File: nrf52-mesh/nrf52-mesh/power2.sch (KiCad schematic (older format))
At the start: 19 parts, among them J4 Conn_01x02_Male, J5 Conn_01x02_Male, U1 TLV62568DBV, U3 FAN5341, U6 CP2102N-A01-GQFN24, X1 USBFCI_10103594

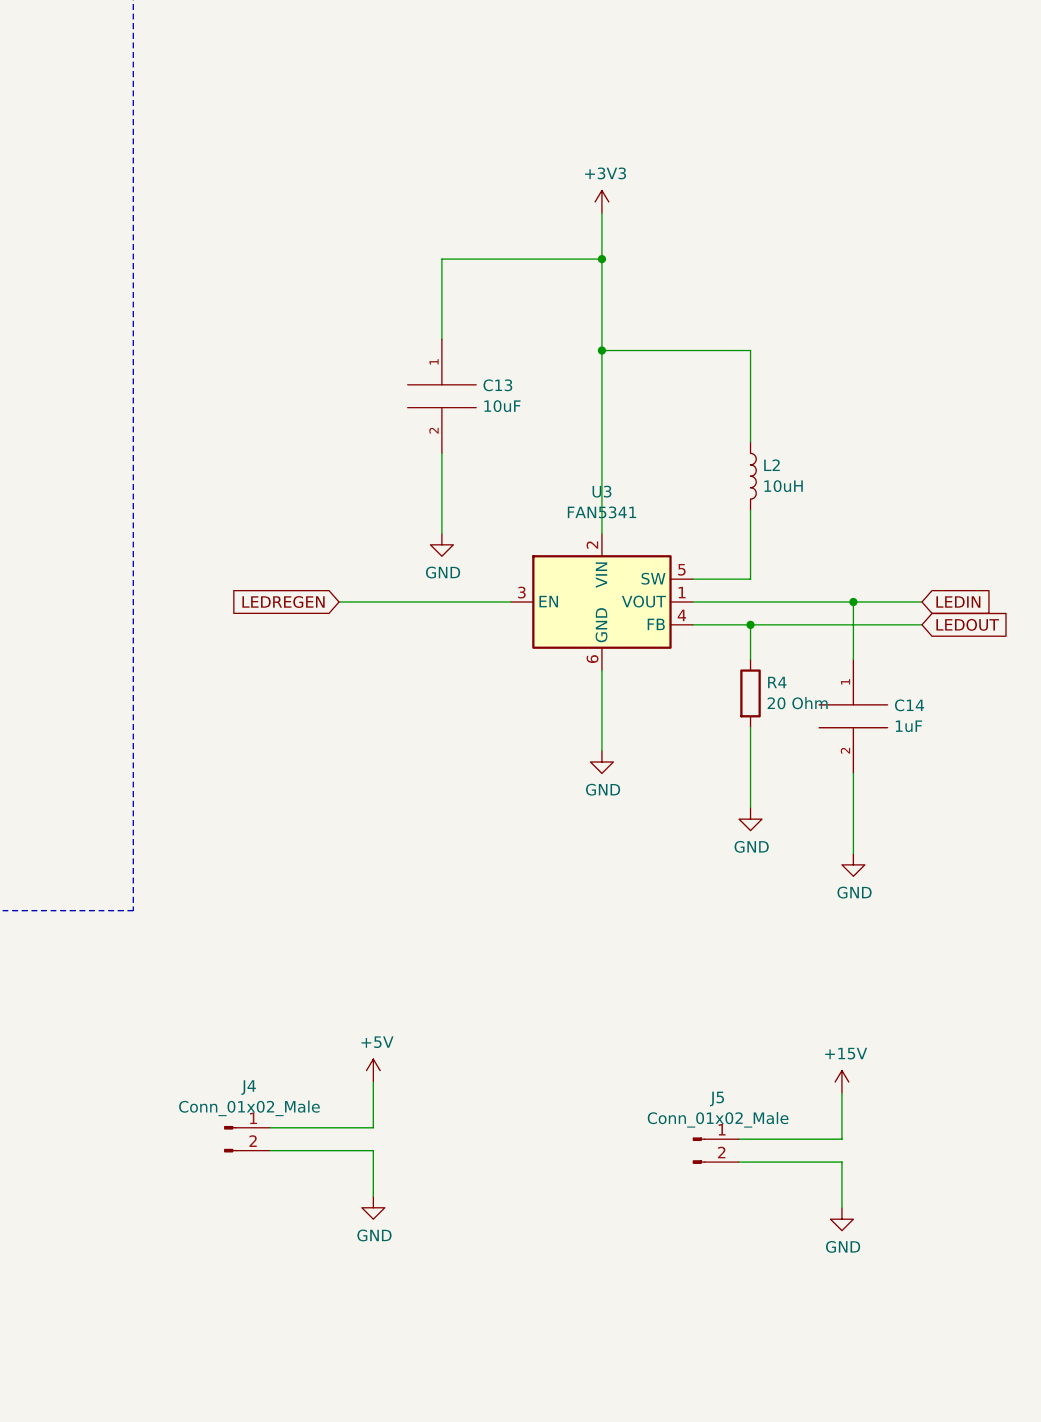
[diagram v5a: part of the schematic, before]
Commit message: nRF52 + ESP WROOM
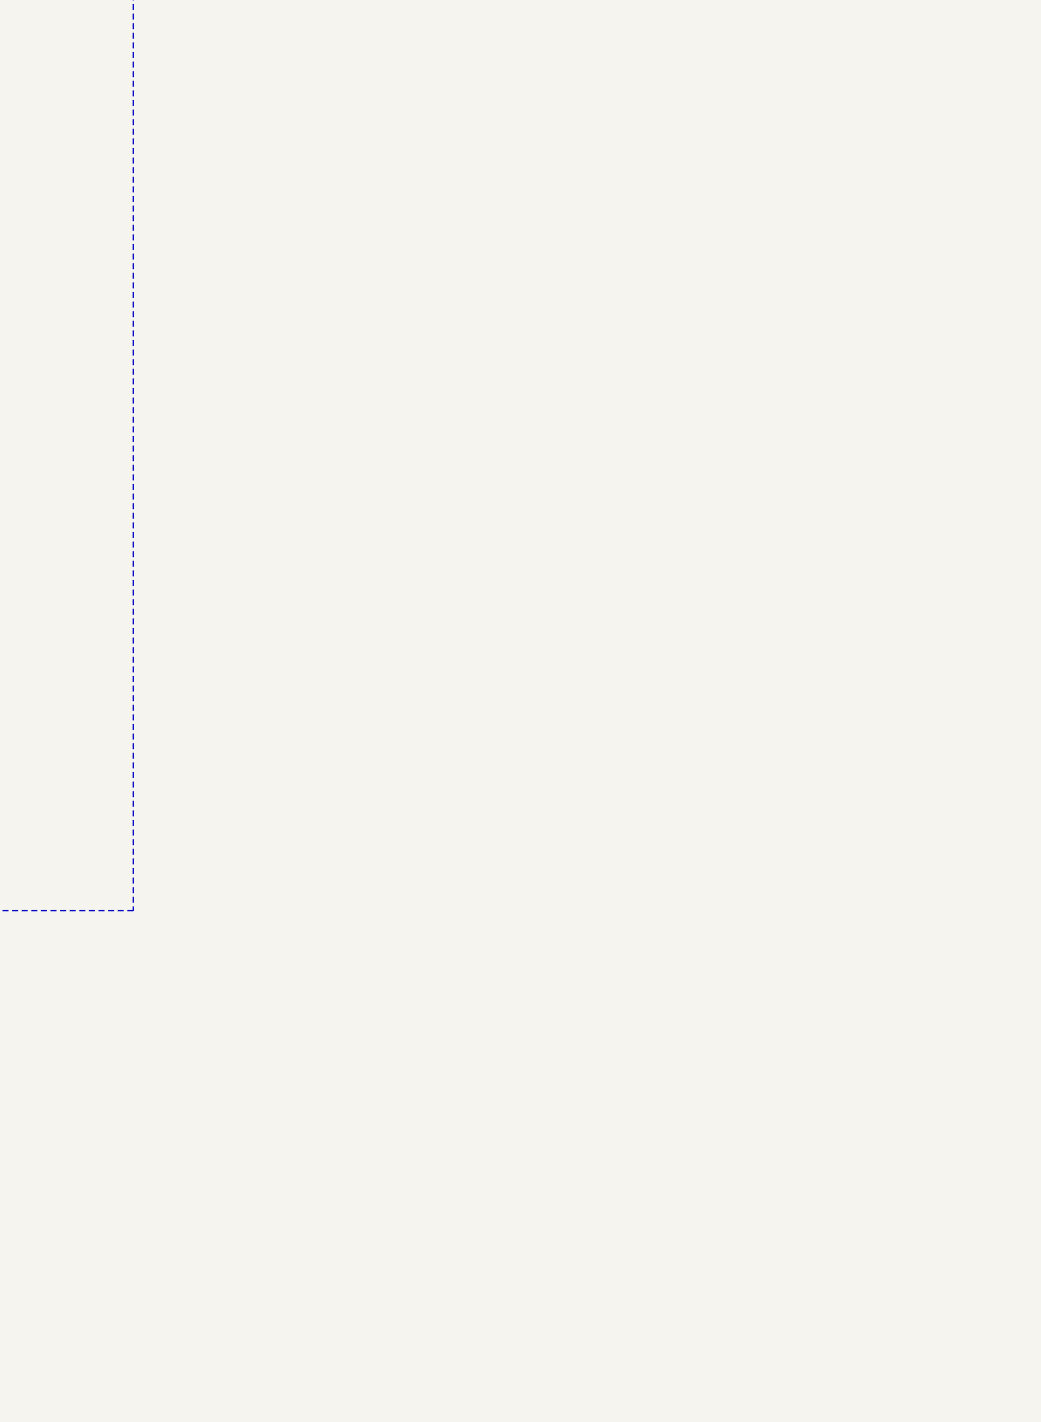
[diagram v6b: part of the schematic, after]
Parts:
- removed C13: 10uF, Capacitor_SMD:C_0603_1608Metric, symbol pspice:C
- removed C14: 1uF, Capacitor_SMD:C_0402_1005Metric, symbol pspice:C
- removed J4, J5: Conn_01x02_Male, Connector_PinHeader_2.54mm:PinHeader_1x02_P2.54mm_Vertical, symbol Connector:Conn_01x02_Male
- removed L2: 10uH, Inductor_SMD:L_0805_2012Metric, symbol Device:L
- removed R4: 20 Ohm, Resistor_SMD:R_0402_1005Metric, symbol Device:R
- removed U3: FAN5341, kifootp:FAN5341, symbol kilib:FAN5341
